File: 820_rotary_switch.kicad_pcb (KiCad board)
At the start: 4 copper layers, 24.5 x 34 mm, 2 parts, among them P4 CONN_01X08, SW2 DP6T-ALPHA-SR2511

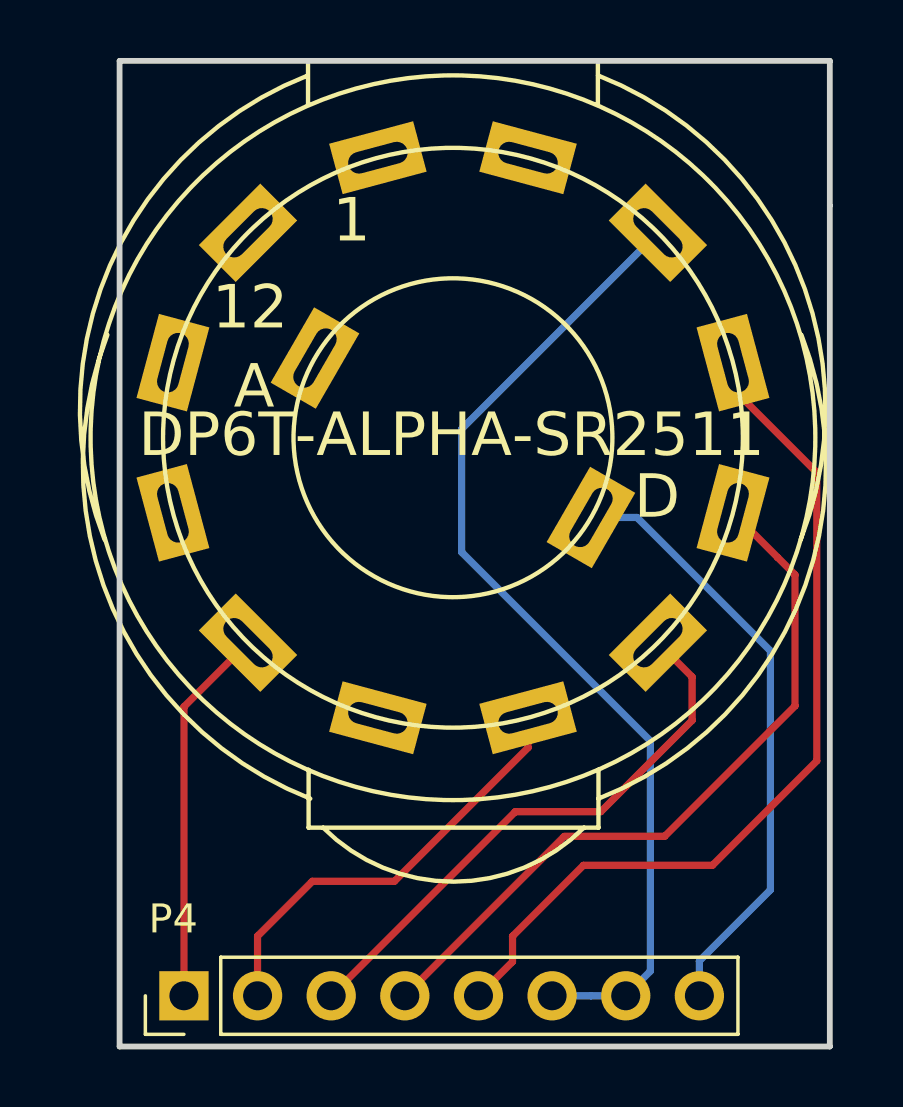
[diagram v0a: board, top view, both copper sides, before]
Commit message: fixed incorrect pin on switch board: 9 was connected instead of 8
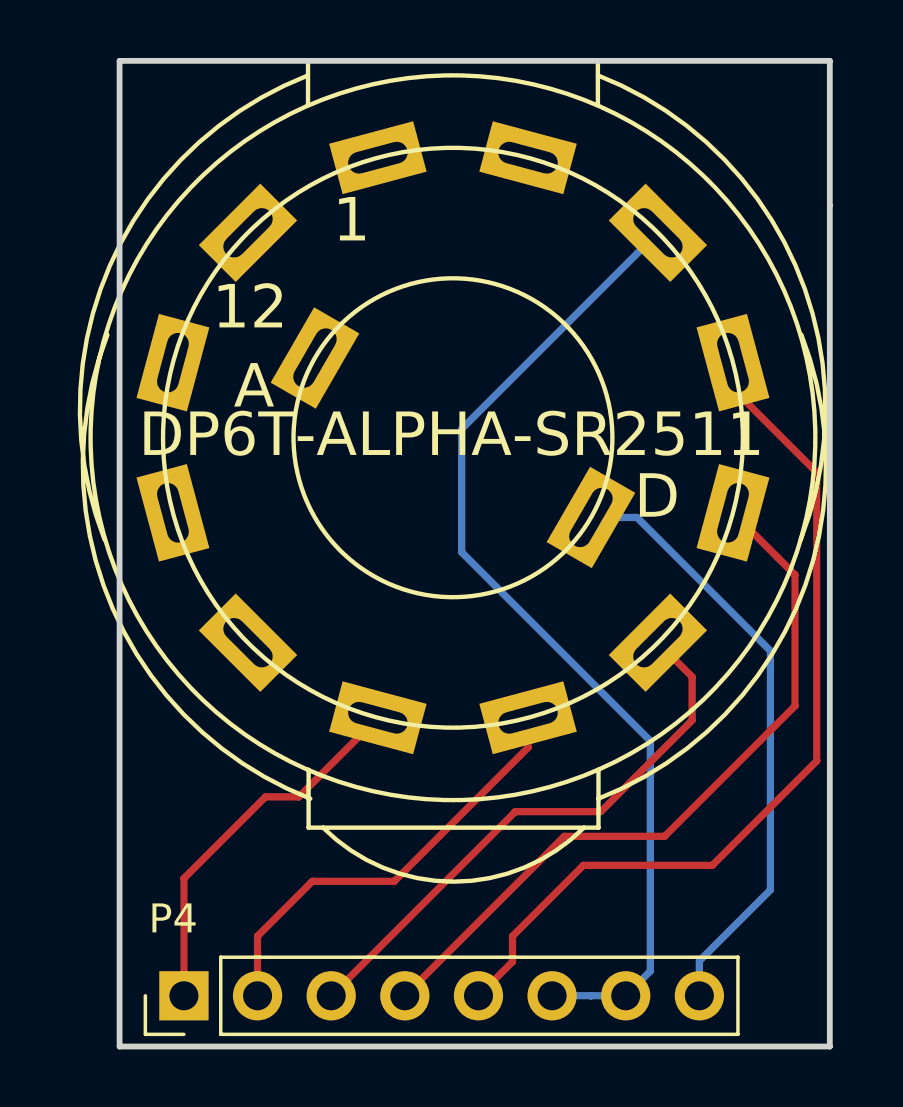
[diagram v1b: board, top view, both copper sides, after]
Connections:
- SW2 pad 8: (no net) -> Net-(P4-Pad1)
- SW2 pad 9: Net-(P4-Pad1) -> (no net)
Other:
- copper layers 4 -> 2
- board text added: "r1.1 10 2018"
- board text removed: "r1.0 08 2018"
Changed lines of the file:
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@@
     (thickness 1.6)
     (drawings 12)
-    (tracks 38)
+    (tracks 40)
     (zones 0)
     (modules 2)
@@
   (layers
     (0 F.Cu signal)
-    (1 In1.Cu mixed)
-    (2 In2.Cu power)
     (31 B.Cu signal)
     (32 B.Adhes user)
@@
     (visible_elements 7FFEF7FF)
     (pcbplotparams
-      (layerselection 0x01400_00000000)
-      (usegerberextensions false)
-      (excludeedgelayer false)
+      (layerselection 0x010f0_80000001)
+      (usegerberextensions true)
+      (excludeedgelayer true)
       (linewidth 0.200000)
       (plotframeref false)
@@
       (plotinvisibletext false)
       (padsonsilk false)
-      (subtractmaskfromsilk false)
-      (outputformat 3)
+      (subtractmaskfromsilk true)
+      (outputformat 1)
       (mirror false)
       (drillshape 0)
@@
     (pad 11 thru_hole rect (at -9.66 -2.59 75) (size 3 1.8) (drill oval 2.1 0.75) (layers *.Cu *.Mask F.SilkS))
     (pad 10 thru_hole rect (at -9.66 2.59 285) (size 3 1.8) (drill oval 2.1 0.75) (layers *.Cu *.Mask F.SilkS))
-    (pad 9 thru_hole rect (at -7.07 7.07 315) (size 3 1.8) (drill oval 2.1 0.75) (layers *.Cu *.Mask F.SilkS)
+    (pad 9 thru_hole rect (at -7.07 7.07 315) (size 3 1.8) (drill oval 2.1 0.75) (layers *.Cu *.Mask F.SilkS))
+    (pad 8 thru_hole rect (at -2.59 9.66 345) (size 3 1.8) (drill oval 2.1 0.75) (layers *.Cu *.Mask F.SilkS)
       (net 1 "Net-(P4-Pad1)"))
-    (pad 8 thru_hole rect (at -2.59 9.66 345) (size 3 1.8) (drill oval 2.1 0.75) (layers *.Cu *.Mask F.SilkS))
     (pad D thru_hole rect (at 4.76 2.75 60) (size 3 1.8) (drill oval 2.25 0.75) (layers *.Cu *.Mask F.SilkS)
       (net 7 "Net-(P4-Pad8)"))
@@
     )
   )
-  (gr_text "r1.0 08 2018" (at 49.5 71) (layer B.SilkS)
+  (gr_text "r1.1 10 2018" (at 49.5 71) (layer B.SilkS)
     (effects (font (size 1 1) (thickness 0.25)) (justify mirror))
   )
@@
   (gr_line (start 49.151091 59.904457) (end 53.151091 59.904457) (layer Eco1.User) (width 0.1))
   (gr_line (start 39.651101 46.953581) (end 39.651101 46.953581) (layer Eco1.User) (width 0.1))
-  (segment (start 41.87 74.15) (end 41.87 64.18) (width 0.25) (layer F.Cu) (net 1))
-  (segment (start 41.87 64.18) (end 44.08 61.97) (width 0.25) (layer F.Cu) (net 1))
+  (segment (start 41.87 74.15) (end 41.87 70.1) (width 0.25) (layer F.Cu) (net 1))
+  (segment (start 41.87 70.1) (end 44.68 67.29) (width 0.25) (layer F.Cu) (net 1))
+  (segment (start 44.68 67.29) (end 45.83 67.29) (width 0.25) (layer F.Cu) (net 1))
+  (segment (start 45.83 67.29) (end 48.56 64.56) (width 0.25) (layer F.Cu) (net 1))
   (segment (start 46.3 70.2) (end 44.41 72.09) (width 0.25) (layer F.Cu) (net 2))
   (segment (start 44.41 72.09) (end 44.41 74.15) (width 0.25) (layer F.Cu) (net 2))

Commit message: gerbers ready to submit to pcb fab house. need to generate gerbers for rotary switch board still
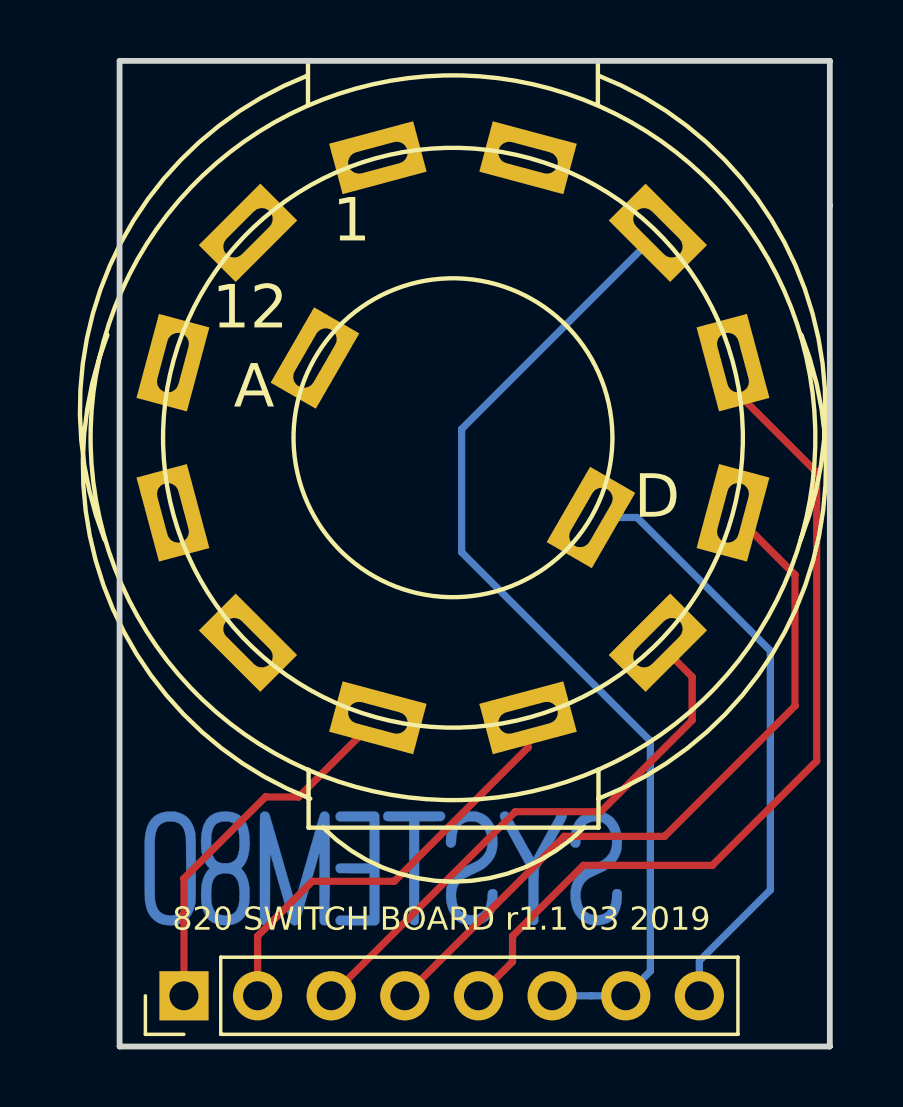
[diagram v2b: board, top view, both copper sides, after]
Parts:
- added G***: LOGO, LOGO, B.Cu at (48.8, 69.8)
- added G***: LOGO, LOGO, B.Cu at (51.1, 54.9)
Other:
- board text added: "820 SWITCH BOARD r1.1 03 2019"
- board text removed: "820 SWITCH BOARD"
- board text removed: "r1.1 10 2018"

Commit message: final prototype ordred, built and tested, committing now and then branching to panelization
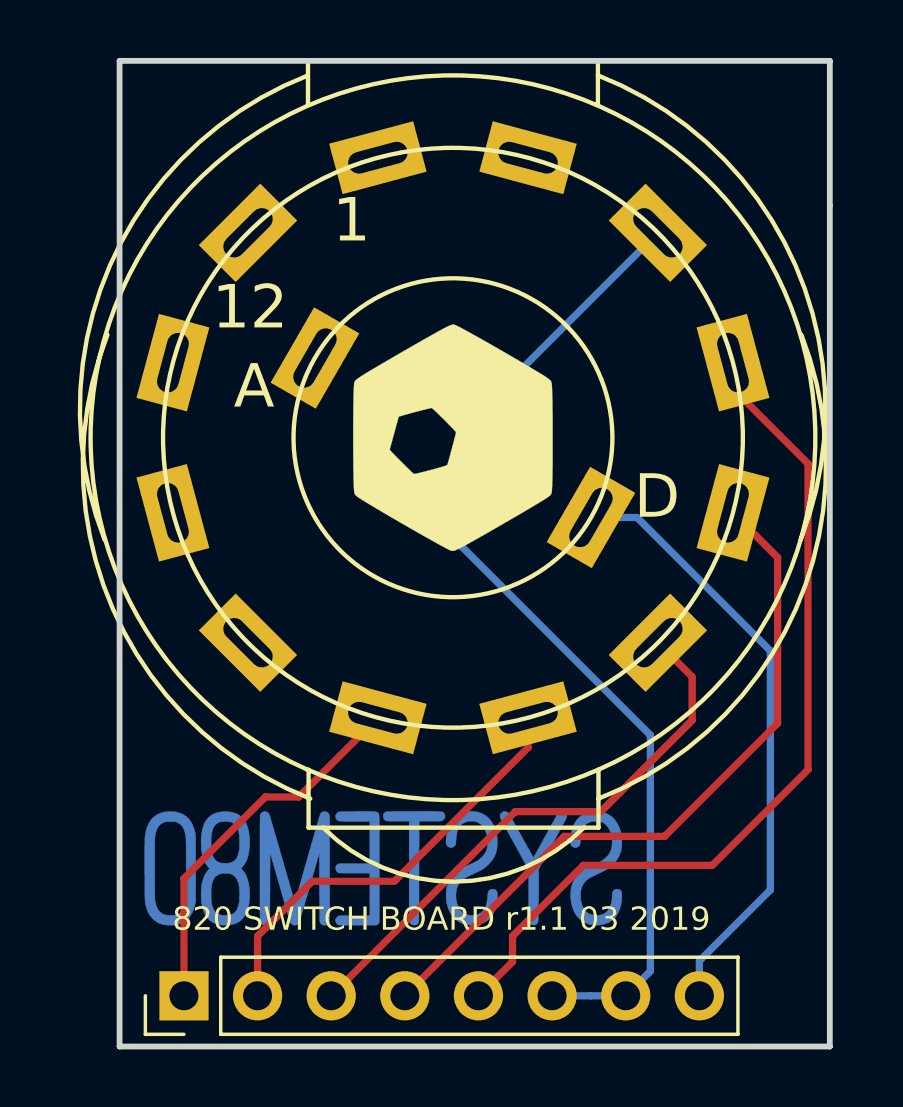
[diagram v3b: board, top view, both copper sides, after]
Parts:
- added G***: LOGO, LOGO, B.Cu at (50.5, 54.9)
- G***: moved to F.Cu
- turned G*** to 75 degrees
